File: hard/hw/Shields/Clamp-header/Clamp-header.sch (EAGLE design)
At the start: 26 parts, among them J1 6p-2.54-90d, J10 6p-SMD-2.54, J11 6p-smd-2.54-90d, J12 6p-2.54-90d, J13 6p-2.54-90d, J14 6p-SMD-2.54, J2 6p-smd-2.54-90d, J3 6p-smd-2.54-90d, J4 6p-SMD-2.54, J5 6p-2.54-90d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

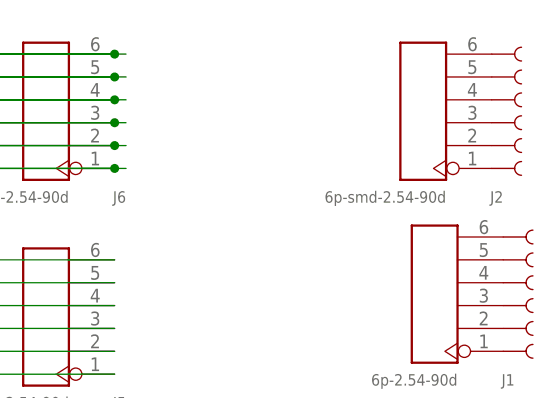
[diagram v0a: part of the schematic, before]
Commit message: Correccion Shield Clamp
by Ruben
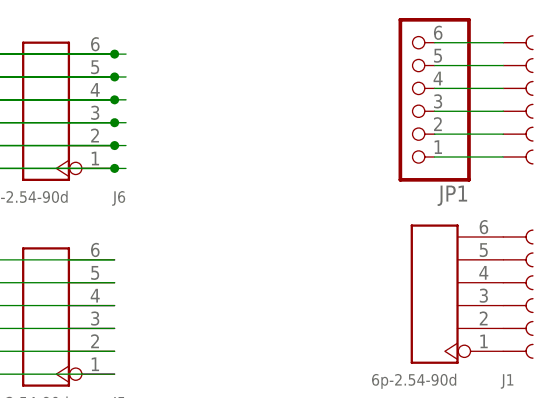
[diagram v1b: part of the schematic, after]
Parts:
- removed J2: 6p-smd-2.54-90d, Seeed-OPL-Connector:SMD-BLACK-MALE-HEADER(6P-2.54-90D)
- added JP1: (no value), pinhead:PINHD-1X6/90
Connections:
- net N$10: now also JP1.3, U$1.1; no longer J2.3, U$7.1
- net N$11: now also JP1.2, U$5.1; no longer J2.2, U$6.1
- net N$12: now also JP1.1, U$2.1; no longer J2.1, U$3.1
- net N$7: now also JP1.6, U$3.1; no longer J2.4, U$1.1
- net N$8: now also JP1.5, U$6.1; no longer J2.6, U$2.1
- net N$9: now also JP1.4, U$7.1; no longer J2.5, U$5.1
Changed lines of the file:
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@@
 <part name="U$6" library="LilyPad-Wearables" deviceset="SEWTAP" device="1"/>
 <part name="U$7" library="LilyPad-Wearables" deviceset="SEWTAP" device="1"/>
-<part name="J2" library="Seeed-OPL-Connector" deviceset="SMD-BLACK-MALE-HEADER(6P-2.54-90D)" device="" value="6p-smd-2.54-90d"/>
 <part name="J3" library="Seeed-OPL-Connector" deviceset="SMD-BLACK-MALE-HEADER(6P-2.54-90D)" device="" value="6p-smd-2.54-90d"/>
 <part name="J5" library="Seeed-OPL-Connector" deviceset="DIP-BLACK-FEMALE-HEADER-R/A(6P-2.54-90D)" device="" value="6p-2.54-90d"/>
@@
 <part name="J13" library="Seeed-OPL-Connector" deviceset="DIP-BLACK-FEMALE-HEADER-R/A(6P-2.54-90D)" device="" value="6p-2.54-90d"/>
 <part name="J14" library="Seeed-OPL-Connector" deviceset="SMD-BLACK-FEMALE-HEADER(6P-2.54)" device="" value="6p-SMD-2.54"/>
+<part name="JP1" library="pinhead" deviceset="PINHD-1X6" device="/90"/>
 </parts>
 <sheets>
@@
 <instance part="U$4" gate="G$1" x="152.4" y="97.79"/>
 <instance part="J1" gate="G$1" x="142.24" y="104.14" rot="R180"/>
-<instance part="U$1" gate="G$1" x="151.13" y="125.73"/>
-<instance part="U$2" gate="G$1" x="151.13" y="130.81"/>
-<instance part="U$3" gate="G$1" x="151.13" y="118.11"/>
-<instance part="U$5" gate="G$1" x="151.13" y="128.27"/>
-<instance part="U$6" gate="G$1" x="151.13" y="120.65"/>
-<instance part="U$7" gate="G$1" x="151.13" y="123.19"/>
-<instance part="J2" gate="G$1" x="140.97" y="124.46" rot="R180"/>
+<instance part="U$1" gate="G$1" x="152.4" y="124.46"/>
+<instance part="U$2" gate="G$1" x="152.4" y="119.38"/>
+<instance part="U$3" gate="G$1" x="152.4" y="132.08"/>
+<instance part="U$5" gate="G$1" x="152.4" y="121.92"/>
+<instance part="U$6" gate="G$1" x="152.4" y="129.54"/>
+<instance part="U$7" gate="G$1" x="152.4" y="127"/>
 <instance part="J3" gate="G$1" x="80.01" y="124.46" rot="R180"/>
 <instance part="J5" gate="G$1" x="99.06" y="101.6" rot="R180"/>
@@
 <instance part="J13" gate="G$1" x="54.61" y="78.74" rot="R180"/>
 <instance part="J14" gate="G$1" x="34.29" y="55.88" rot="R180"/>
+<instance part="JP1" gate="A" x="139.7" y="127" rot="R180"/>
 </instances>
 <busses>
@@
 <pinref part="J1" gate="G$1" pin="1"/>
 <pinref part="U$4" gate="G$1" pin="1"/>
-</segment>
-</net>
-<net name="N$7" class="0">
-<segment>
-<pinref part="J2" gate="G$1" pin="4"/>
-<pinref part="U$1" gate="G$1" pin="1"/>
-</segment>
-</net>
-<net name="N$8" class="0">
-<segment>
-<pinref part="J2" gate="G$1" pin="6"/>
-<pinref part="U$2" gate="G$1" pin="1"/>
-</segment>
-</net>
-<net name="N$9" class="0">
-<segment>
-<pinref part="J2" gate="G$1" pin="5"/>
-<pinref part="U$5" gate="G$1" pin="1"/>
-</segment>
-</net>
-<net name="N$10" class="0">
-<segment>
-<pinref part="J2" gate="G$1" pin="3"/>
-<pinref part="U$7" gate="G$1" pin="1"/>
-</segment>
-</net>
-<net name="N$11" class="0">
-<segment>
-<pinref part="J2" gate="G$1" pin="2"/>
-<pinref part="U$6" gate="G$1" pin="1"/>
-</segment>
-</net>
-<net name="N$12" class="0">
-<segment>
-<pinref part="J2" gate="G$1" pin="1"/>
-<pinref part="U$3" gate="G$1" pin="1"/>
 </segment>
 </net>
@@
 </segment>
 </net>
+<net name="N$7" class="0">
+<segment>
+<pinref part="U$3" gate="G$1" pin="1"/>
+<pinref part="JP1" gate="A" pin="6"/>
+<wire x1="149.86" y1="132.08" x2="142.24" y2="132.08" width="0.1524" layer="91"/>
+</segment>
+</net>
+<net name="N$8" class="0">
+<segment>
+<pinref part="U$6" gate="G$1" pin="1"/>
+<pinref part="JP1" gate="A" pin="5"/>
+<wire x1="149.86" y1="129.54" x2="142.24" y2="129.54" width="0.1524" layer="91"/>
+</segment>
+</net>
+<net name="N$9" class="0">
+<segment>
+<pinref part="U$7" gate="G$1" pin="1"/>
+<pinref part="JP1" gate="A" pin="4"/>
+<wire x1="149.86" y1="127" x2="142.24" y2="127" width="0.1524" layer="91"/>
+</segment>
+</net>
+<net name="N$10" class="0">
+<segment>
+<pinref part="U$1" gate="G$1" pin="1"/>
+<pinref part="JP1" gate="A" pin="3"/>
+<wire x1="149.86" y1="124.46" x2="142.24" y2="124.46" width="0.1524" layer="91"/>
+</segment>
+</net>
+<net name="N$11" class="0">
+<segment>
+<pinref part="U$5" gate="G$1" pin="1"/>
+<pinref part="JP1" gate="A" pin="2"/>
+<wire x1="149.86" y1="121.92" x2="142.24" y2="121.92" width="0.1524" layer="91"/>
+</segment>
+</net>
+<net name="N$12" class="0">
+<segment>
+<pinref part="U$2" gate="G$1" pin="1"/>
+<pinref part="JP1" gate="A" pin="1"/>
+<wire x1="149.86" y1="119.38" x2="142.24" y2="119.38" width="0.1524" layer="91"/>
+</segment>
+</net>
